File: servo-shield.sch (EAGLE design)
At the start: 30 parts, among them IC1 24AA01P, K1 PIN20X2

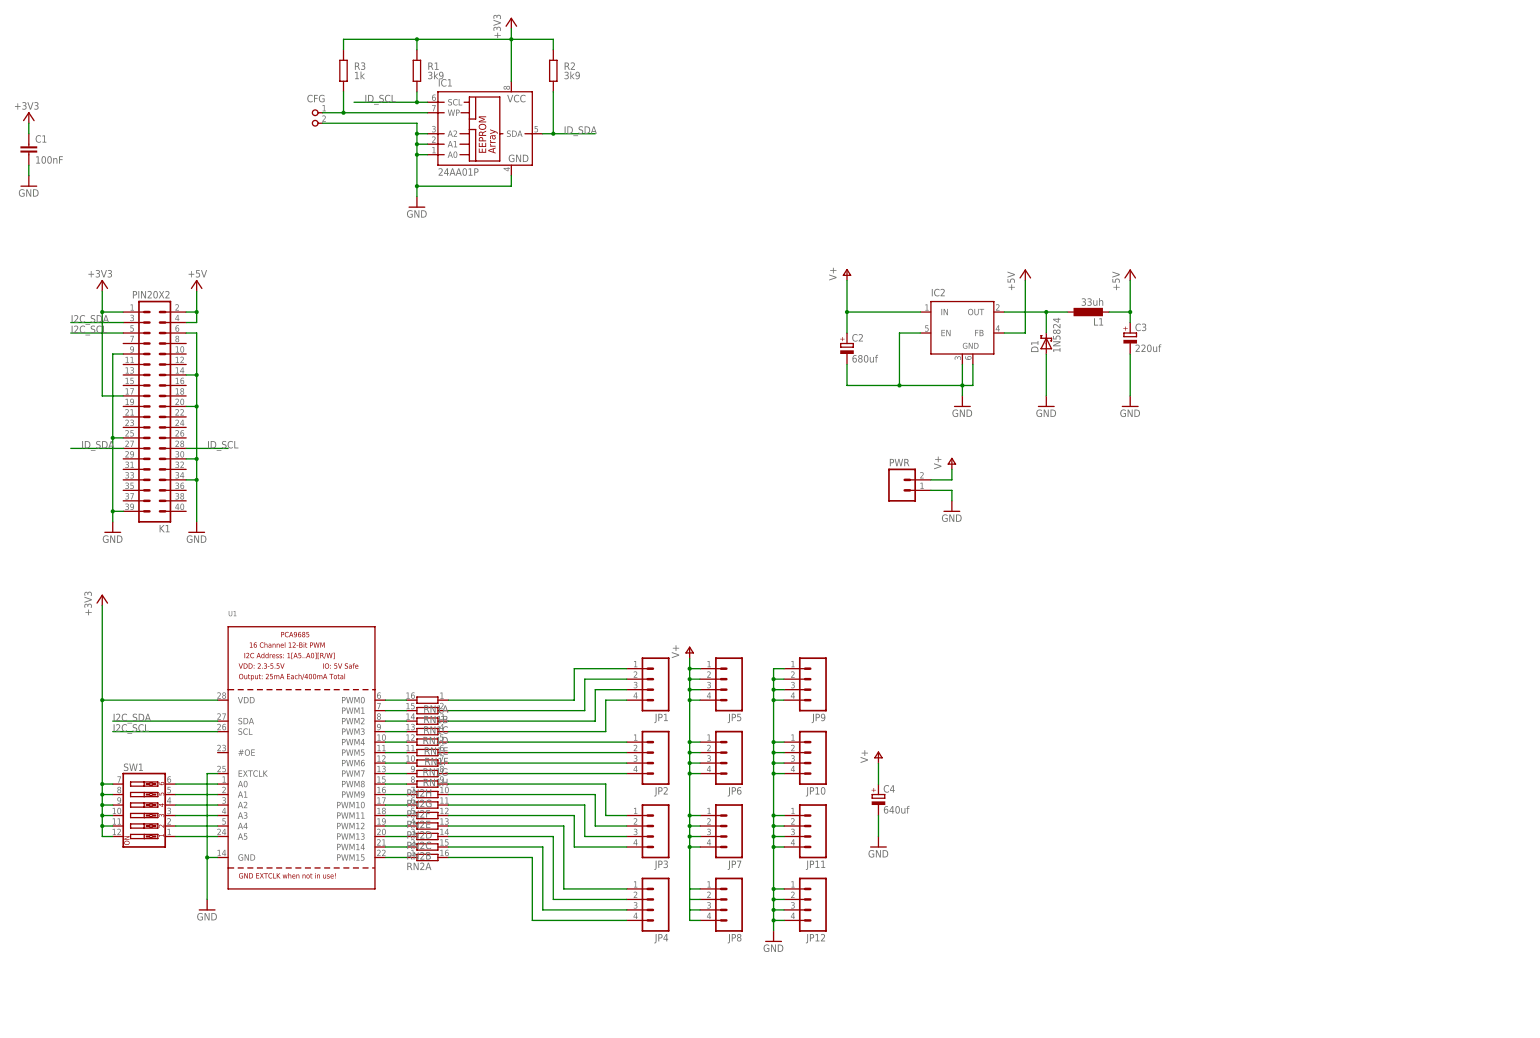
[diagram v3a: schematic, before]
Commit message: Mk2 board. Move servo connectors to longer edge, remove HAT related crap. We're not using it anyway, its just i2c. Fixed issues with regulator using a bogus inductor. Fixed power connector. Hopefully fixed clearance issues with standoffs. Fixed clearance issue with soldering 40 pin connector hitting previous resistor networks. Use more SMD parts to reduce PCB used space. This WILL require a stencil.
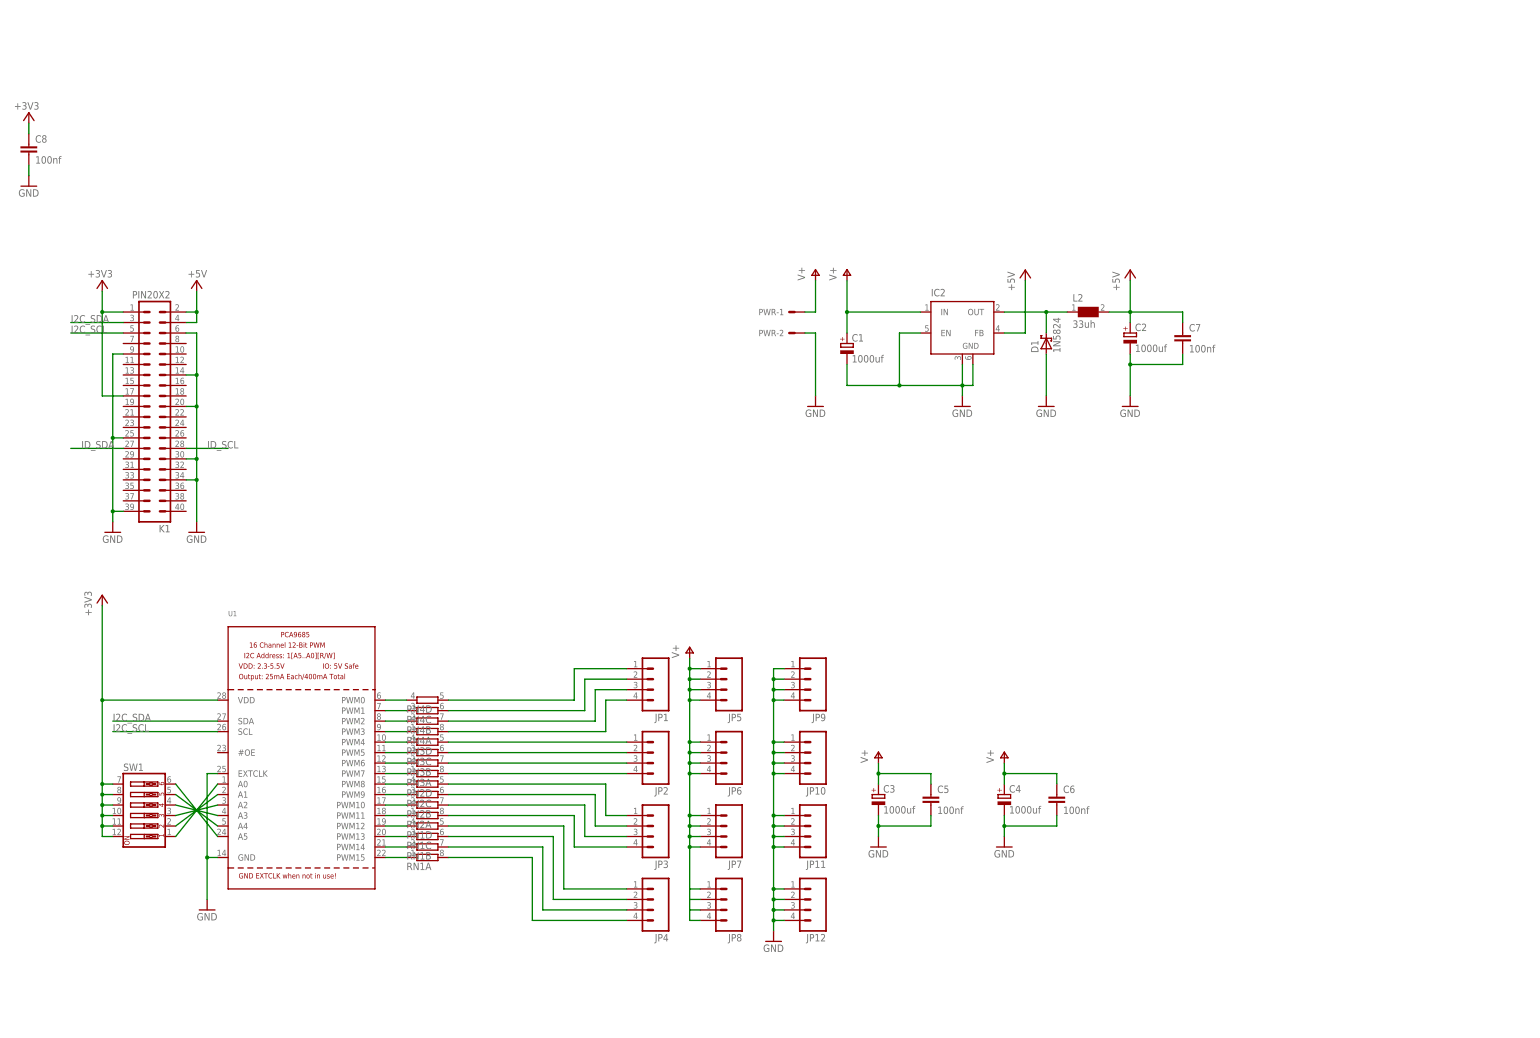
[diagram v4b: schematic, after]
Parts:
- removed CFG: (no value), FLYFISH:PIN2_100
- removed IC1: 24AA01P, microchip:24AA01P
- removed L1: 33uh, rcl:L-EU0207/10
- removed R1, R2: 3k9, rcl:R-EU_0204/7
- removed R3: 1k, rcl:R-EU_0204/7
- added C5, C6, C7, C8: 100nf, rcl:C-EU025-030X050
- added L2: 33uh, WE-PD:WE-PD-744770133_1260/1245/1280/1210
- added RN3, RN4: (no value), resistor-dil:4R-NEXB38V
- C1: value 100nF -> 1000uf; device rcl:C-EU025-030X050 -> rcl:CPOL-EUE3.5-8; DIELECTRIC X7R -> (none)
- C2: value 680uf -> 1000uf; device rcl:CPOL-EUE2.5-6 -> rcl:CPOL-EUE3.5-8
- C3: value 220uf -> 1000uf; device rcl:CPOL-EUE2.5-6 -> rcl:CPOL-EUE3.5-8
- C4: value 640uf -> 1000uf; device rcl:CPOL-EUE2.5-6 -> rcl:CPOL-EUE3.5-8
- PWR: value M02JST-PTH-2 -> 22-05-7028-02; device SparkFun-Connectors:M02JST-PTH-2 -> con-molex:22-05-7028-02
- RN1, RN2: device resistor-dil:8R-N -> resistor-dil:4R-NEXB38V
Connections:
- removed net N$16: SW1.6, U1.A0
- removed net N$40: D1.C, IC2.OUT, L1.1
- new net VOUT: D1.C, IC2.OUT, L2.1
- net +3V3: now also C8.1; no longer C1.1, IC1.VCC, R1.2, R2.2, R3.2
- net +5V: now also C2.+, C7.1, L2.2; no longer C3.+, L1.2
- net GND: now also C1.-, C5.2, C6.2, C7.2, C8.2, PWR-2.S; no longer C1.2, CFG.2, IC1.A0, IC1.A1, IC1.A2, IC1.GND, PWR.1
- net ID_SCL: no longer IC1.SCL, R1.1
- net ID_SDA: no longer IC1.SDA, R2.1
- net N$1: now also RN2C.1; no longer RN2G.1
- net N$10: now also RN2C.2; no longer RN2G.2
- net N$11: now also U1.A0; no longer U1.A5
- net N$12: now also U1.A1; no longer U1.A4
- net N$13: now also SW1.5, U1.A4; no longer SW1.3, U1.A3
- net N$14: now also SW1.3; no longer SW1.4
- net N$15: now also SW1.4, U1.A3; no longer SW1.5, U1.A1
- net N$17: now also RN2B.2; no longer RN2F.2
- net N$18: now also RN2A.2; no longer RN2E.2
- net N$19: now also RN1D.2; no longer RN2D.2
- net N$2: now also RN2D.1; no longer RN2H.1
- net N$20: now also RN1C.2; no longer RN2C.2
- net N$21: now also RN1B.2; no longer RN2B.2
- net N$22: now also RN1A.2; no longer RN2A.2
- net N$23: now also RN1A.1; no longer RN2A.1
- net N$24: now also RN1B.1; no longer RN2B.1
- net N$25: now also RN1C.1; no longer RN2C.1
- net N$26: now also RN1D.1; no longer RN2D.1
- net N$27: now also RN2A.1; no longer RN2E.1
- net N$28: now also RN2B.1; no longer RN2F.1
- net N$29: now also RN3B.1; no longer RN1G.2
- net N$3: now also RN3A.1; no longer RN1H.2
- net N$30: now also RN3C.1; no longer RN1F.2
- net N$31: now also RN3D.1; no longer RN1E.2
- net N$32: now also RN4A.1; no longer RN1D.2
- net N$33: now also RN4B.1; no longer RN1C.2
- net N$34: now also RN4C.1; no longer RN1B.2
- net N$35: now also RN4D.1; no longer RN1A.2
- net N$36: now also RN3D.2; no longer RN1E.1
- net N$37: now also RN3A.2; no longer RN1H.1
- net N$38: now also RN3B.2; no longer RN1G.1
- net N$39: now also RN3C.2; no longer RN1F.1
- net N$4: now also SW1.6, U1.A5; no longer CFG.1, IC1.WP, R3.1
- net N$5: now also RN4A.2; no longer RN1D.1
- net N$6: now also RN4B.2; no longer RN1C.1
- net N$7: now also RN4C.2; no longer RN1B.1
- net N$8: now also RN4D.2; no longer RN1A.1
- net N$9: now also RN2D.2; no longer RN2H.2
- net V+: now also C1.+, C3.+, C5.1, C6.1, PWR-1.S; no longer C2.+, PWR.2
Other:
- moved on the sheet: C2, C3, C4, RN1A, RN1B, RN1C, RN1D, RN2A, RN2B, RN2C, RN2D

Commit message: Rejig schematic to fit on an A4 schematic sheet
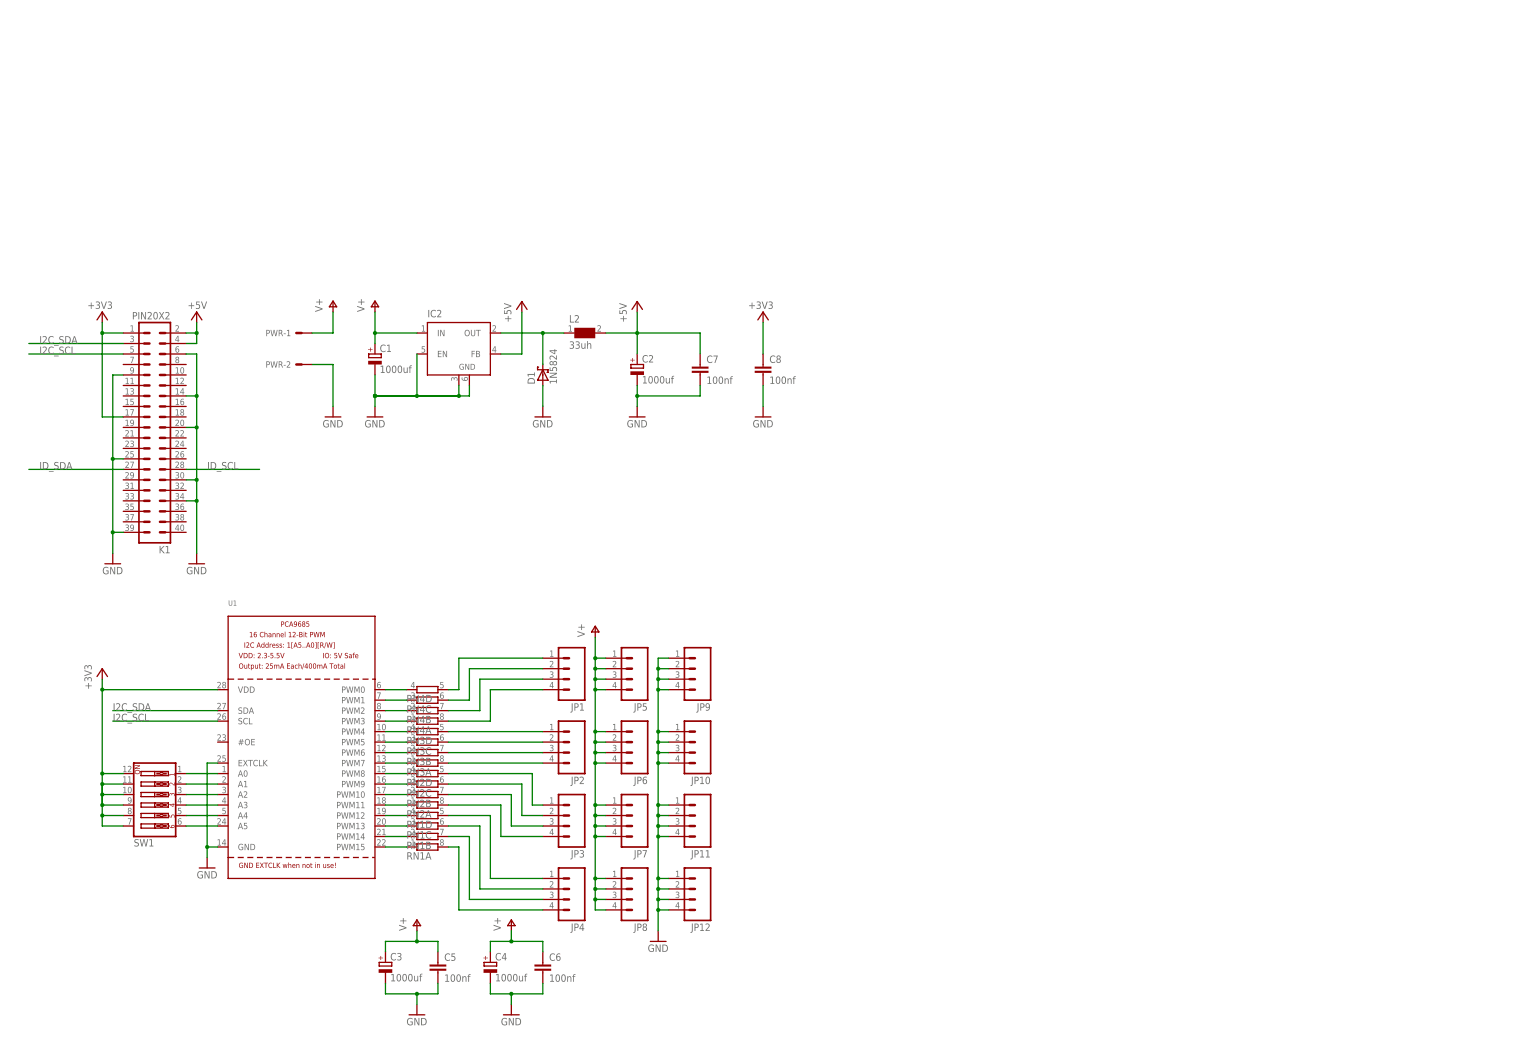
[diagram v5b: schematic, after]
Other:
- moved on the sheet: C1, C2, C3, C4, C5, C6, C7, C8, D1, IC2, JP1, JP10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

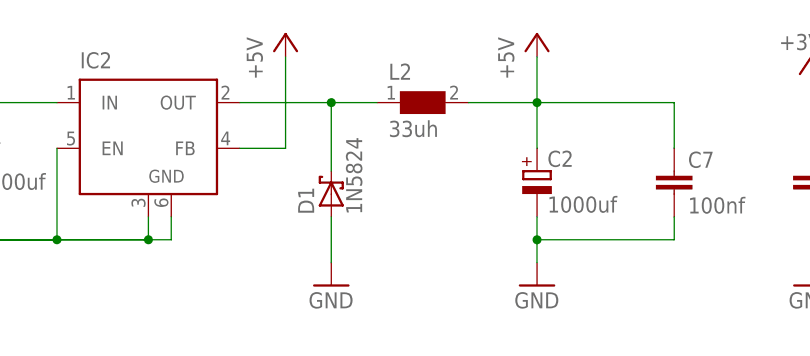
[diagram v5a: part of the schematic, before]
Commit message: Move some parts labels about
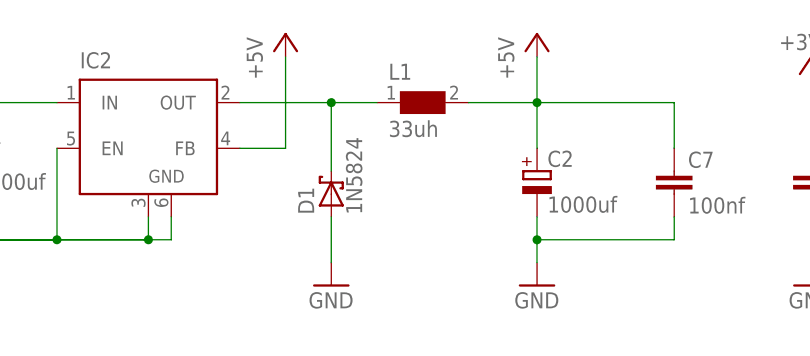
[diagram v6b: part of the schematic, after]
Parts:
- renumbered L2 to L1
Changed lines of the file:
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@@
 <part name="P+7" library="supply1" deviceset="V+" device=""/>
 <part name="GND11" library="supply1" deviceset="GND" device=""/>
-<part name="L2" library="WE-PD" deviceset="WE-PD" device="_1260/1245/1280/1210" technology="-744770133" value="33uh"/>
+<part name="L1" library="WE-PD" deviceset="WE-PD" device="_1260/1245/1280/1210" technology="-744770133" value="33uh"/>
 <part name="C2" library="rcl" deviceset="CPOL-EU" device="E3.5-8" value="1000uf"/>
 <part name="C3" library="rcl" deviceset="CPOL-EU" device="E3.5-8" value="1000uf"/>
@@
 <instance part="P+7" gate="1" x="93.98" y="177.8"/>
 <instance part="GND11" gate="1" x="93.98" y="149.86"/>
-<instance part="L2" gate="G$1" x="154.94" y="170.18"/>
+<instance part="L1" gate="G$1" x="154.94" y="170.18"/>
 <instance part="C2" gate="G$1" x="167.64" y="162.56"/>
 <instance part="C3" gate="G$1" x="106.68" y="17.78"/>
@@
 <wire x1="167.64" y1="165.1" x2="167.64" y2="170.18" width="0.1524" layer="91"/>
 <junction x="167.64" y="170.18"/>
-<pinref part="L2" gate="G$1" pin="2"/>
+<pinref part="L1" gate="G$1" pin="2"/>
 <pinref part="C2" gate="G$1" pin="+"/>
 <pinref part="C7" gate="G$1" pin="1"/>
@@
 <pinref part="D1" gate="G$1" pin="C"/>
 <junction x="144.78" y="170.18"/>
-<pinref part="L2" gate="G$1" pin="1"/>
-</segment>
-</net>
+<pinref part="L1" gate="G$1" pin="1"/>
+</segment>
+</net>

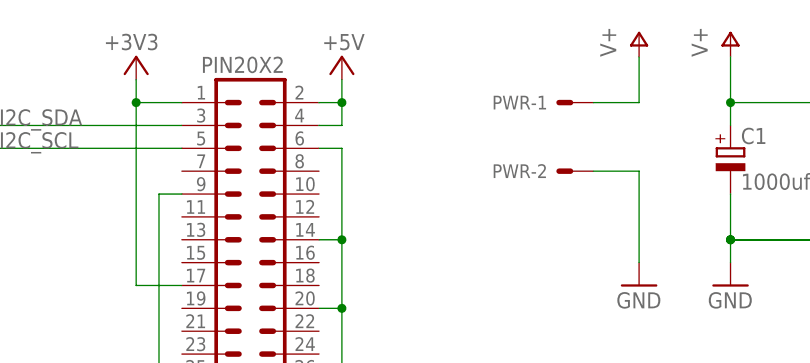
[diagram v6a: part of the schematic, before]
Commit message: add jumper to select if RaspberryPi uses servo board regulator.
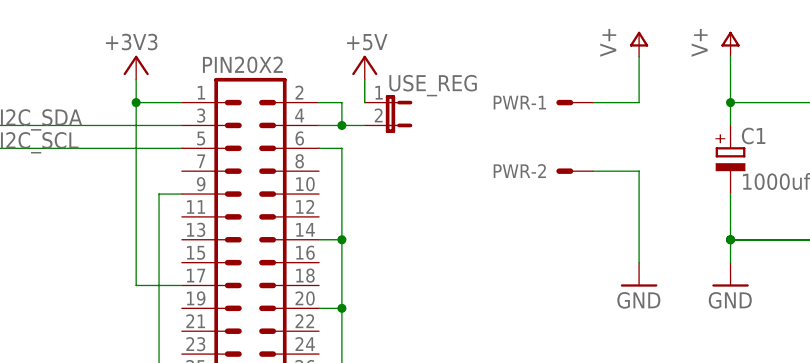
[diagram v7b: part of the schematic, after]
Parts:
- added USE_REG: (no value), jumper:JP1E
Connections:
- new net N$16: K1.2, K1.4, USE_REG.2
- net +5V: now also USE_REG.1; no longer K1.2, K1.4
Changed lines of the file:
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@@
 <part name="C6" library="rcl" deviceset="C-EU" device="025-030X050" value="100nf"/>
 <part name="FRAME1" library="frames" deviceset="DINA4_L" device=""/>
+<part name="USE_REG" library="jumper" deviceset="JP1E" device=""/>
 </parts>
 <sheets>
@@
 <instance part="GND2" gate="1" x="198.12" y="149.86"/>
 <instance part="GND3" gate="1" x="40.64" y="114.3"/>
-<instance part="P+1" gate="1" x="60.96" y="175.26" smashed="yes">
-<attribute name="VALUE" x="63.5" y="177.8" size="1.778" layer="96" rot="R180"/>
+<instance part="P+1" gate="1" x="63.5" y="175.26" smashed="yes">
+<attribute name="VALUE" x="66.04" y="177.8" size="1.778" layer="96" rot="R180"/>
 </instance>
 <instance part="U1" gate="G$1" x="86.36" y="68.58"/>
@@
 <instance part="FRAME1" gate="G$1" x="0" y="0"/>
 <instance part="FRAME1" gate="G$2" x="0" y="0"/>
+<instance part="USE_REG" gate="A" x="66.04" y="170.18" rot="R270"/>
 </instances>
 <busses>
@@
 <net name="+5V" class="0">
 <segment>
-<pinref part="K1" gate="G$1" pin="2"/>
-<pinref part="P+1" gate="1" pin="+5V"/>
-<wire x1="58.42" y1="170.18" x2="60.96" y2="170.18" width="0.1524" layer="91"/>
-<wire x1="60.96" y1="170.18" x2="60.96" y2="172.72" width="0.1524" layer="91"/>
-<pinref part="K1" gate="G$1" pin="4"/>
-<wire x1="58.42" y1="167.64" x2="60.96" y2="167.64" width="0.1524" layer="91"/>
-<wire x1="60.96" y1="167.64" x2="60.96" y2="170.18" width="0.1524" layer="91"/>
-<junction x="60.96" y="170.18"/>
-</segment>
-<segment>
 <pinref part="P+2" gate="1" pin="+5V"/>
 <wire x1="167.64" y1="170.18" x2="167.64" y2="175.26" width="0.1524" layer="91"/>
@@
 <wire x1="134.62" y1="165.1" x2="139.7" y2="165.1" width="0.1524" layer="91"/>
 <wire x1="139.7" y1="165.1" x2="139.7" y2="175.26" width="0.1524" layer="91"/>
+</segment>
+<segment>
+<pinref part="USE_REG" gate="A" pin="1"/>
+<wire x1="63.5" y1="170.18" x2="63.5" y2="172.72" width="0.1524" layer="91"/>
+<pinref part="P+1" gate="1" pin="+5V"/>
 </segment>
 </net>
@@
 </segment>
 </net>
+<net name="N$16" class="0">
+<segment>
+<pinref part="K1" gate="G$1" pin="2"/>
+<wire x1="58.42" y1="170.18" x2="60.96" y2="170.18" width="0.1524" layer="91"/>
+<pinref part="K1" gate="G$1" pin="4"/>
+<wire x1="58.42" y1="167.64" x2="60.96" y2="167.64" width="0.1524" layer="91"/>
+<wire x1="60.96" y1="167.64" x2="60.96" y2="170.18" width="0.1524" layer="91"/>
+<pinref part="USE_REG" gate="A" pin="2"/>
+<wire x1="60.96" y1="167.64" x2="63.5" y2="167.64" width="0.1524" layer="91"/>
+<junction x="60.96" y="167.64"/>
+</segment>
+</net>
